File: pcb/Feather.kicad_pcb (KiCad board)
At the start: 2 copper layers, 57 x 22.9 mm, 39 parts, among them J1 10118192, J2 S2B-PH-SM4-TB, J3 ANT, J4 U.FL-R-SMT-1, J5 Conn_01x03, J6 Conn_01x12, J7 Conn_01x16, SW1 KMR2, U1 ATSAMD21G18A-M, U2 AP2112K-3.3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

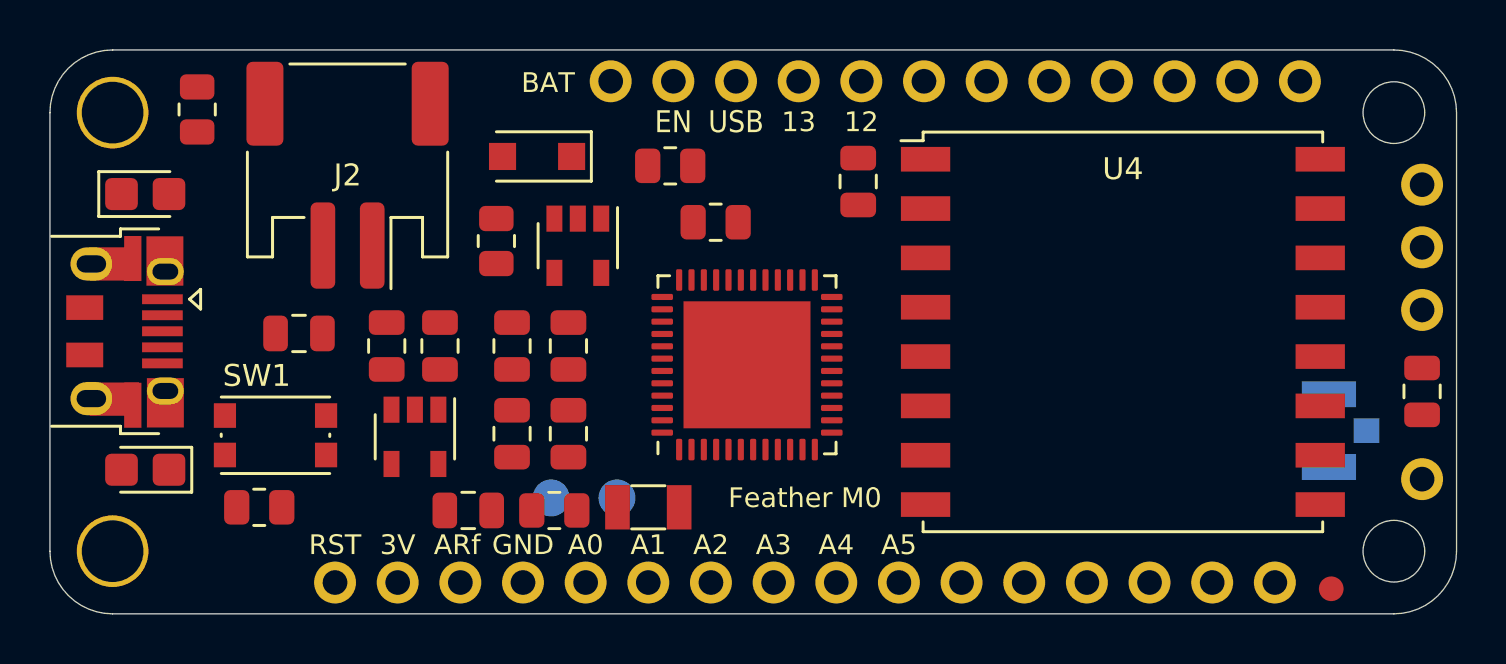
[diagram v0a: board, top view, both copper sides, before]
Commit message: Se corrigen las observaciones realizadas por el docente. Adicionalmente se sube el ruteo de la placa.
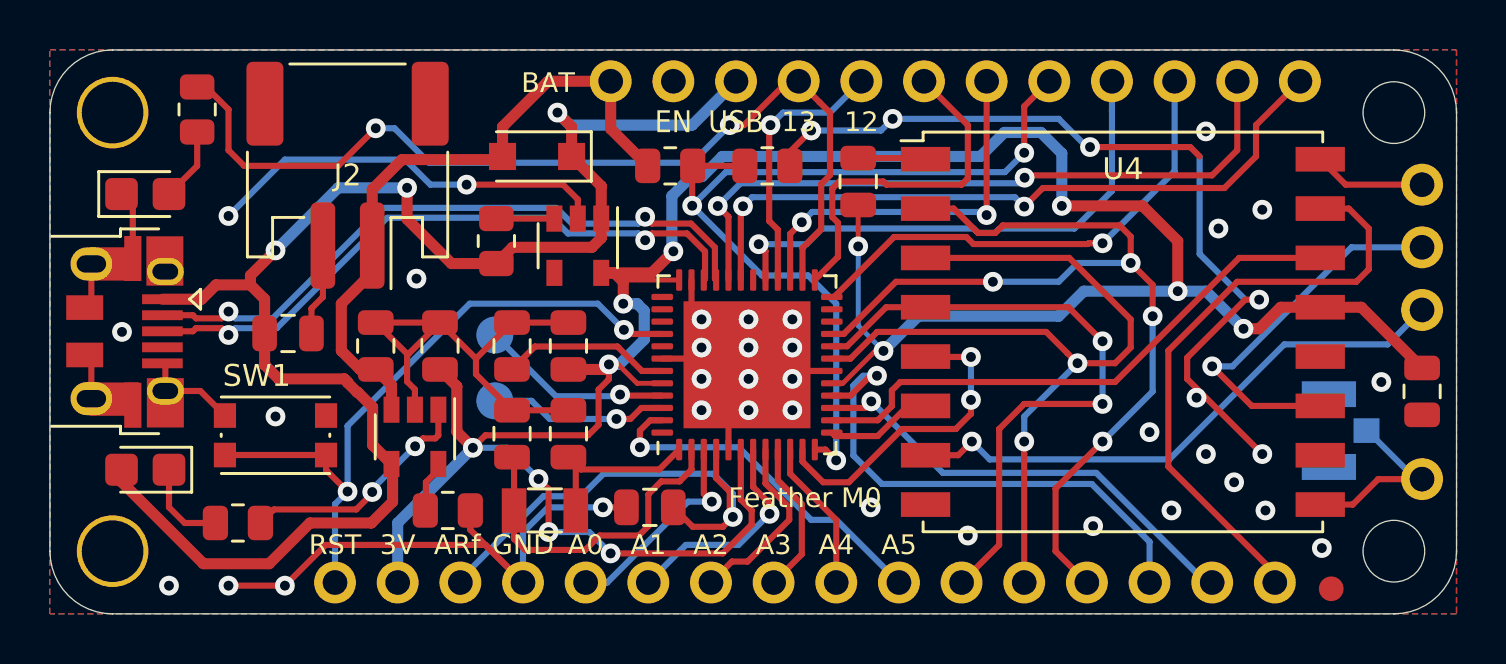
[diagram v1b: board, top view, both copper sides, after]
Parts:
- moved C4 7.36 mm to (138.5, 98.0), turned to 0 degrees
- moved TP1 6.99 mm to (132.2, 91.1), turned to 270 degrees
- moved TP2 6.33 mm to (132.2, 93.7), turned to 270 degrees
- moved R4 4.32 mm to (130.3, 98.2), turned to 0 degrees
- moved Y1 4.19 mm to (134.2, 98.2)
- moved R6 3.10 mm to (143.3, 84.2)
- moved R3 1.07 mm to (121.8, 98.7)
- moved C9 0.44 mm to (127.4, 91.5)
- moved C5 0.44 mm to (123.8, 91.0)
- turned C6 to 90 degrees
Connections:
- net /D2 renamed Net-(U1-Pad23)
- net /D7 renamed Net-(U1-Pad30)
- U1 pad 49: Net-(U1-Pad49) -> GND
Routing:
- net GND: track 0.00 -> 127.4 mm, vias 0 -> 40
- net +3V3: track 0.00 -> 115.0 mm, vias 0 -> 12
- net VBUS: track 0.00 -> 63.0 mm, vias 0 -> 3
- net /MISO: track 0.00 -> 38.9 mm, vias 0 -> 4
- net /D13: track 0.00 -> 38.3 mm, vias 0 -> 2
- net /D9: track 0.00 -> 36.3 mm, vias 0 -> 3
- net /MOSI: track 0.00 -> 33.6 mm, vias 0 -> 2
- net /SDA: track 0.00 -> 28.8 mm, vias 0 -> 2
- net /SCL: track 0.00 -> 28.0 mm, vias 0 -> 2
- net /~RESET: track 0.00 -> 27.8 mm, vias 0 -> 2
- net +BATT: track 0.00 -> 26.9 mm
- net /D-: track 0.00 -> 26.8 mm, vias 0 -> 2
- net /SCK: track 0.00 -> 26.2 mm, vias 0 -> 2
- net /D+: track 0.00 -> 26.1 mm, vias 0 -> 2
- net /DIO1: track 0.00 -> 24.6 mm
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- added copper zone on B.Cu, net GND
- added copper zone on F.Cu, net GND
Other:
- net class Power added: clearance 0.2, trace_width 0.45, via_dia 0.8, via_drill 0.4
- net class USB Data added: clearance 0.15, trace_width 0.25, via_dia 0.8, via_drill 0.4
- board text added: "5) Differential pair: 0,25 mm /0,15 mm (9,84 mils /5,90 mils)"

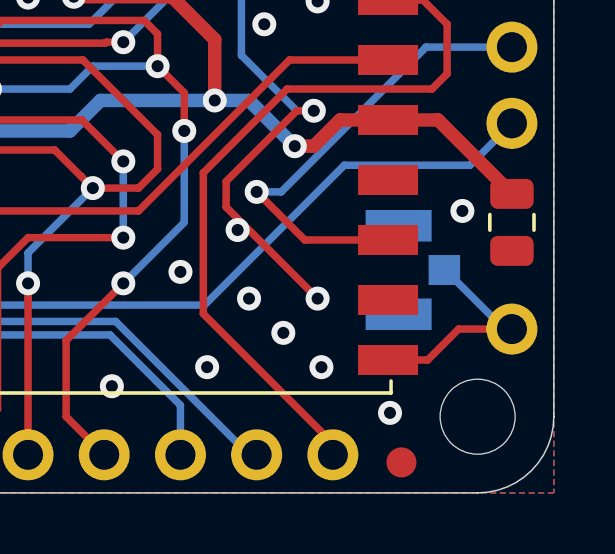
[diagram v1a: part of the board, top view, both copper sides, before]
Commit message: Se modifica la CPW de la línea de antena y se agrega el cálculo.
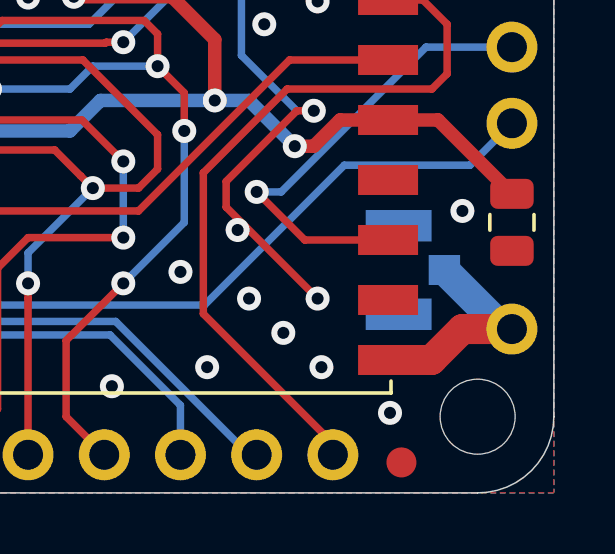
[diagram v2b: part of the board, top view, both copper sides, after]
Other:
- net class CPW added: clearance 0.2, trace_width 1, via_dia 0.8, via_drill 0.4

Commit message: Últimos retoques en el PCB de acuerdo a las correcciones realizadas.
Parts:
- added FID2: Fiducial, Fiducial:Fiducial_1mm_Mask2mm, F.Cu at (132.2, 80.8)
- J1: value 10118192 -> MicroUSB
- J4: value U.FL-R-SMT-1 -> U.FL
- U1: value ATSAMD21G18A-M -> ATSAMD21G18A
- U3: value MCP73831T-2ACI/OT -> MCP73831T
- U4: value RFM95W-915S2 -> RFM95W
- moved J4 0.06 mm to (166.5, 95.0)
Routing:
- net GND: vias 40 -> 44
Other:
- board text added: "+20 dBm"
- board text added: "2) Minimum general clearance: 0,2 mm (7,87 mils)."
- board text added: "3.7/4.2V LiPoly Battery USB Charge"
- board text added: "4) Minimum track width: 0,2 mm (7,87 mils)."
- board text added: "5) Differential pair: 0,25 mm/0,15 mm (9,84 mils/5,90 mils)."
- board text added: "6) CPWG antenna line: 1 mm/0,2 mm (39,37 mils/7,87 mils)."
- board text added: "7) Designed according to Mayer Circuitos Impresos fabrication capabilities."
- board text added: "8) It was required to use 0805 as the minimum acceptable size for all components. For that reason, this design is 6,223 mm longer that the original one."
- board text added: "9) For compatibility reasons, PCB height can't be modified."
- board text added: "ANT"
- board text added: "D2"
- board text added: "D3"
- board text added: "D5"
- board text added: "Designed in Argentina"
- board text added: "Feather M0 RFM9x Radio Module ATSAMD21G18 3.3V"
- board text added: "Frequency"
- board text added: "Node #:"
- board text added: "RF radio uses: MISO/MOSI/SCK 4 RST, 3 IRQ, 8 CS"
- board text added: "RFM9x LoRa"
- board text added: "Rev: A"
- board text removed: "2) Minimum clearance: 0,2 mm (7,87 mils)."
- board text removed: "4) Minimum track size: 0,2 mm (7,87 mils)."
- board text removed: "5) Designed according to Mayer Circuitos Impresos fabrication capabilities."
- board text removed: "5) Differential pair: 0,25 mm /0,15 mm (9,84 mils /5,90 mils)"
- board text removed: "6) It was required to use 0805 as the minimum acceptable size for all components. For that reason, this design is 6,223 mm longer that the original desing."
- board text removed: "7) PCB size may be subject to change after the routing process starts."
- board text removed: "8) For compatibility reasons, PCB height can't be modified."
